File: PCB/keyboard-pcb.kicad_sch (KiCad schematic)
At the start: 181 parts, among them J1 Conn_01x05_Pin, U1 Raspberry_Pi_Pico

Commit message: Modified JOURNAL.md
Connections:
- net Row 2: now also U1.24 (GPIO18); no longer U1.23 (GND)
- net Row 3: now also U1.25 (GPIO19); no longer U1.24 (GPIO18)
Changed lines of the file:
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@@
 	(global_label "Row 3"
 		(shape input)
-		(at 60.96 64.77 0)
+		(at 60.96 62.23 0)
 		(fields_autoplaced yes)
 		(effects
@@
 		)
 		(property "Intersheetrefs" "${INTERSHEET_REFS}"
-			(at 69.8718 64.77 0)
+			(at 69.8718 62.23 0)
 			(effects
 				(font
@@
 	(global_label "Row 2"
 		(shape input)
-		(at 60.96 67.31 0)
+		(at 60.96 64.77 0)
 		(fields_autoplaced yes)
 		(effects
@@
 		)
 		(property "Intersheetrefs" "${INTERSHEET_REFS}"
-			(at 69.8718 67.31 0)
+			(at 69.8718 64.77 0)
 			(effects
 				(font

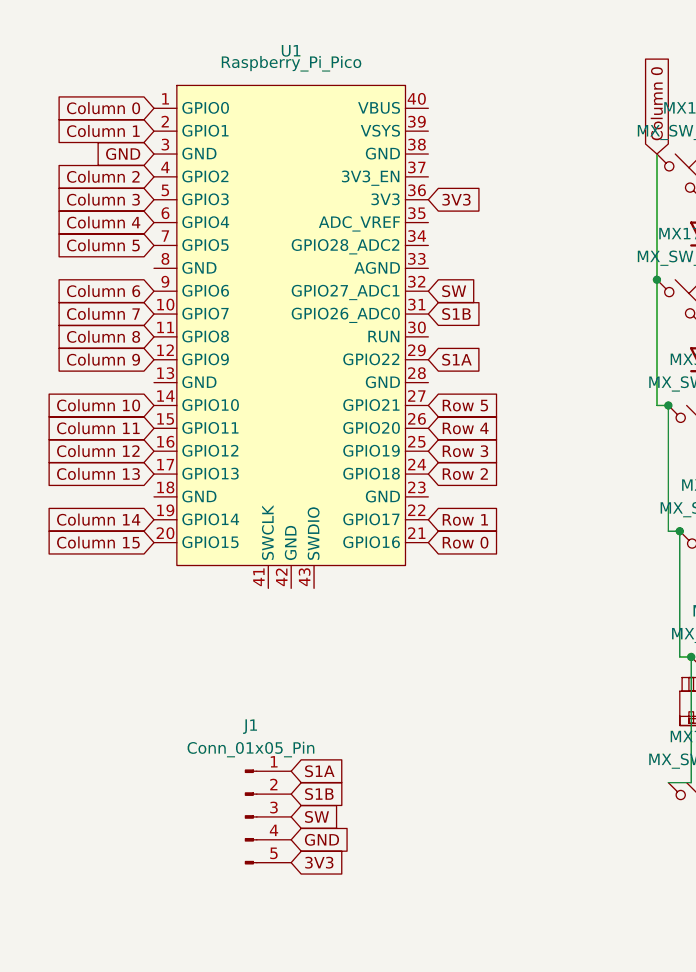
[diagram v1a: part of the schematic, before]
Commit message: Modified whole case, added accents (jinx from arcane reference), connected all gnd pins
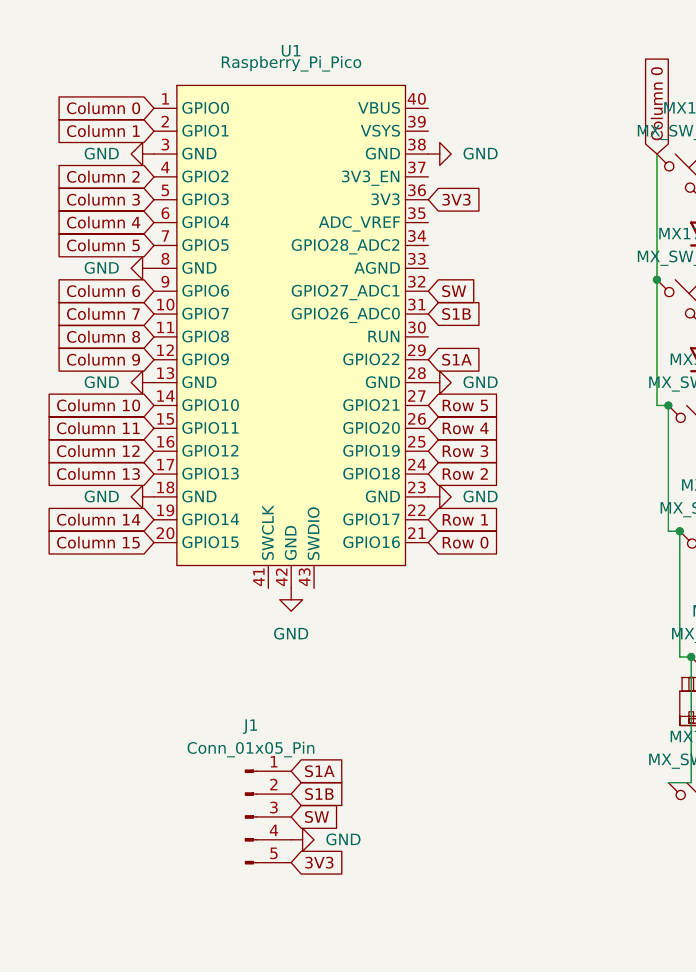
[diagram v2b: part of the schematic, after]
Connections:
- net GND: now also U1.13 (GND), U1.18 (GND), U1.23 (GND), U1.28 (GND), U1.38 (GND), U1.42 (GND), U1.8 (GND)

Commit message: fixed stuff ig
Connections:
- net Column 16: now also U1.34 (GPIO28_ADC2)
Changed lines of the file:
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@@
+		)
+	)
+	(global_label "Column 16"
+		(shape input)
+		(at 60.96 39.37 0)
+		(fields_autoplaced yes)
+		(effects
+			(font
+				(size 1.27 1.27)
+			)
+			(justify left)
+		)
+		(property "Intersheetrefs" "${INTERSHEET_REFS}"
+			(at 74.4073 39.37 0)
+			(effects
+				(font
+					(size 1.27 1.27)
+				)
+				(justify left)
+				(hide yes)
+			)
 		)
 	)
